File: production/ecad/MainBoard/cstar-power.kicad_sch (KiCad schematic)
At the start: 48 parts, among them IC1 LT8648SEV#PBF, J1 Conn_01x02_Pin, J2 Conn_01x02_Pin, J3 Conn_01x02_Pin, J4 XT60PW-M, U1 AZ1117IH-3.3TRG1

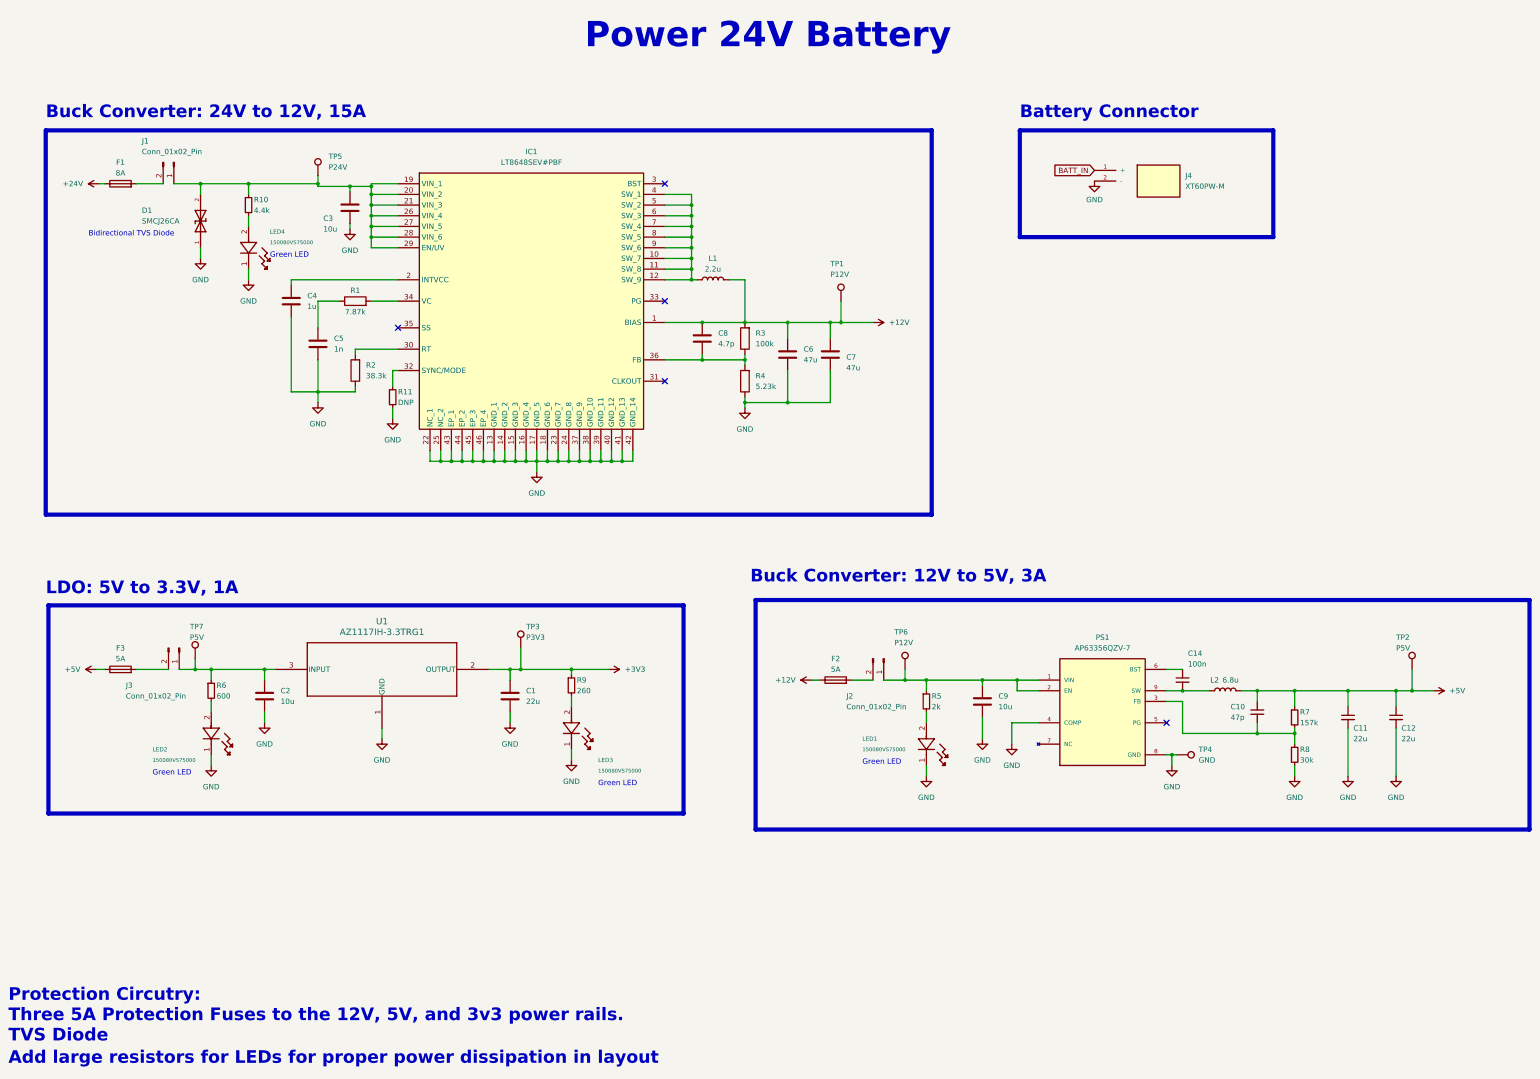
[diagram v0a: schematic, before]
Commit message: changed the path of the footprints and changed the name of the test points
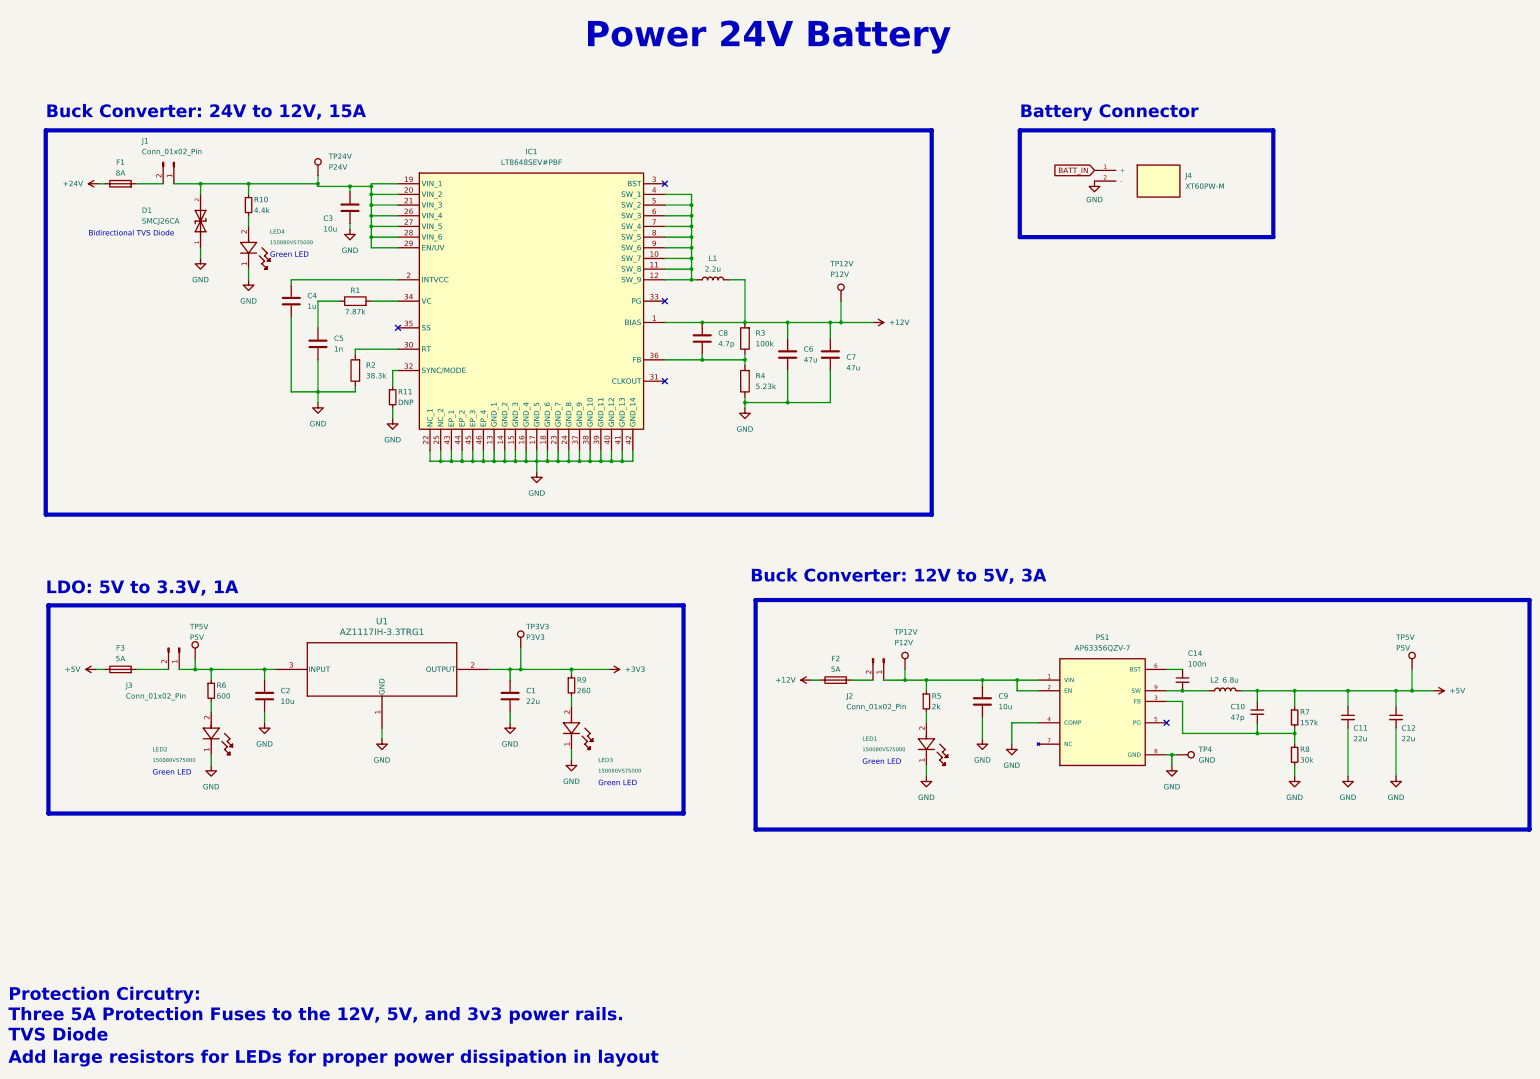
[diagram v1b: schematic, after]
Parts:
- IC1: footprint LT8648SEVPBF -> (none)
- LED1, LED2, LED3, LED4: footprint LED_0VS75000_WRE -> 150080VS75000:LED_0VS75000_WRE
- U1: footprint SOT223_AZ1117I_6P5X3P5_DIO -> AZ1117IH-3.3TRG1:SOT230P700X185-4N
- renumbered TP1 to TP12V, TP6 to TP12V, TP5 to TP24V, TP3 to TP3V3, TP2 to TP5V, TP7 to TP5V
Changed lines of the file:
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@@
       (effects (font (size 0.9 0.9)) (justify left))
     )
-    (property "Footprint" "LED_0VS75000_WRE" (at 242.57 187.96 0)
+    (property "Footprint" "150080VS75000:LED_0VS75000_WRE" (at 242.57 187.96 0)
       (effects (font (size 1.27 1.27) italic) hide)
     )
@@
   (symbol (lib_id "Connector:TestPoint") (at 97.79 57.785 0) (unit 1)
     (in_bom yes) (on_board yes) (dnp no) (fields_autoplaced)
-    (property "Reference" "TP5" (at 100.33 53.213 0)
+    (property "Reference" "TP24V" (at 100.33 53.213 0)
       (effects (font (size 1.27 1.27)) (justify left))
     )
@@
       (project "cstar-power"
         (path "/7edd775e-47a6-46f9-8e16-808bdf3a0e15"
-          (reference "TP5") (unit 1)
+          (reference "TP24V") (unit 1)
         )
       )
@@
   (symbol (lib_id "Connector:TestPoint") (at 222.25 87.63 0) (unit 1)
     (in_bom yes) (on_board yes) (dnp no)
-    (property "Reference" "TP1" (at 219.71 78.74 0)
+    (property "Reference" "TP12V" (at 219.71 78.74 0)
       (effects (font (size 1.27 1.27)) (justify left))
     )
@@
       (project "cstar-power"
         (path "/7edd775e-47a6-46f9-8e16-808bdf3a0e15"
-          (reference "TP1") (unit 1)
+          (reference "TP12V") (unit 1)
         )
       )
@@
       (effects (font (size 1.524 1.524)))
     )
-    (property "Footprint" "SOT223_AZ1117I_6P5X3P5_DIO" (at 83.82 154.94 0)
+    (property "Footprint" "AZ1117IH-3.3TRG1:SOT230P700X185-4N" (at 83.82 154.94 0)
       (effects (font (size 1.27 1.27) italic) hide)
     )
@@
       (effects (font (size 1.27 1.27)))
     )
-    (property "Footprint" "LT8648SEVPBF" (at 176.53 154.61 0)
+    (property "Footprint" "" (at 176.53 154.61 0)
       (effects (font (size 1.27 1.27)) (justify left top) hide)
     )
@@
   (symbol (lib_id "Connector:TestPoint") (at 146.05 170.18 0) (unit 1)
     (in_bom yes) (on_board yes) (dnp no)
-    (property "Reference" "TP3" (at 147.32 165.1 0)
+    (property "Reference" "TP3V3" (at 147.32 165.1 0)
       (effects (font (size 1.27 1.27)) (justify left))
     )
@@
       (project "cstar-power"
         (path "/7edd775e-47a6-46f9-8e16-808bdf3a0e15"
-          (reference "TP3") (unit 1)
+          (reference "TP3V3") (unit 1)
         )
       )
@@
       (effects (font (size 0.9 0.9)) (justify left))
     )
-    (property "Footprint" "LED_0VS75000_WRE" (at 158.115 184.15 0)
+    (property "Footprint" "150080VS75000:LED_0VS75000_WRE" (at 158.115 184.15 0)
       (effects (font (size 1.27 1.27) italic) hide)
     )
@@
   (symbol (lib_id "Connector:TestPoint") (at 358.14 175.26 0) (unit 1)
     (in_bom yes) (on_board yes) (dnp no)
-    (property "Reference" "TP2" (at 354.33 167.64 0)
+    (property "Reference" "TP5V" (at 354.33 167.64 0)
       (effects (font (size 1.27 1.27)) (justify left))
     )
@@
       (project "cstar-power"
         (path "/7edd775e-47a6-46f9-8e16-808bdf3a0e15"
-          (reference "TP2") (unit 1)
+          (reference "TP5V") (unit 1)
         )
       )
@@
       (effects (font (size 0.9 0.9)) (justify left))
     )
-    (property "Footprint" "LED_0VS75000_WRE" (at 72.39 185.42 0)
+    (property "Footprint" "150080VS75000:LED_0VS75000_WRE" (at 72.39 185.42 0)
       (effects (font (size 1.27 1.27) italic) hide)
     )
@@
       (effects (font (size 0.9 0.9)) (justify left))
     )
-    (property "Footprint" "LED_0VS75000_WRE" (at 81.28 69.85 0)
+    (property "Footprint" "150080VS75000:LED_0VS75000_WRE" (at 81.28 69.85 0)
       (effects (font (size 1.27 1.27) italic) hide)
     )
@@
   (symbol (lib_id "Connector:TestPoint") (at 68.58 172.72 0) (unit 1)
     (in_bom yes) (on_board yes) (dnp no)
-    (property "Reference" "TP7" (at 67.31 165.1 0)
+    (property "Reference" "TP5V" (at 67.31 165.1 0)
       (effects (font (size 1.27 1.27)) (justify left))
     )
@@
       (project "cstar-power"
         (path "/7edd775e-47a6-46f9-8e16-808bdf3a0e15"
-          (reference "TP7") (unit 1)
+          (reference "TP5V") (unit 1)
         )
       )
@@
   (symbol (lib_id "Connector:TestPoint") (at 237.49 175.26 0) (unit 1)
     (in_bom yes) (on_board yes) (dnp no)
-    (property "Reference" "TP6" (at 234.95 166.37 0)
+    (property "Reference" "TP12V" (at 234.95 166.37 0)
       (effects (font (size 1.27 1.27)) (justify left))
     )
@@
       (project "cstar-power"
         (path "/7edd775e-47a6-46f9-8e16-808bdf3a0e15"
-          (reference "TP6") (unit 1)
-        )
-      )
+          (reference "TP12V") (unit 1)
+        )
+      )

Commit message: footprint assignments
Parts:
- IC1: footprint (none) -> CSTAR-MainBoard-Footprints:MODULE_ESP32-WROOM-32UE_M113EH6400UH3Q0_
- LED1, LED2, LED3, LED4: footprint 150080VS75000:LED_0VS75000_WRE -> (none)
- PS1: footprint AP63356QZV-7:CONV_AP63356QZV-7 -> CSTAR-MainBoard-Footprints:USBCONN-GCT_USB4105GFA
- U1: footprint AZ1117IH-3.3TRG1:SOT230P700X185-4N -> (none)
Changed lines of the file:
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@@
       (effects (font (size 0.9 0.9)) (justify left))
     )
-    (property "Footprint" "150080VS75000:LED_0VS75000_WRE" (at 242.57 187.96 0)
+    (property "Footprint" "" (at 242.57 187.96 0)
       (effects (font (size 1.27 1.27) italic) hide)
     )
@@
       (effects (font (size 1.524 1.524)))
     )
-    (property "Footprint" "AZ1117IH-3.3TRG1:SOT230P700X185-4N" (at 83.82 154.94 0)
+    (property "Footprint" "" (at 83.82 154.94 0)
       (effects (font (size 1.27 1.27) italic) hide)
     )
@@
       (effects (font (size 1.27 1.27)))
     )
-    (property "Footprint" "" (at 176.53 154.61 0)
+    (property "Footprint" "CSTAR-MainBoard-Footprints:MODULE_ESP32-WROOM-32UE_M113EH6400UH3Q0_" (at 176.53 154.61 0)
       (effects (font (size 1.27 1.27)) (justify left top) hide)
     )
@@
       (effects (font (size 1.27 1.27)))
     )
-    (property "Footprint" "AP63356QZV-7:CONV_AP63356QZV-7" (at 284.48 185.42 0)
+    (property "Footprint" "CSTAR-MainBoard-Footprints:USBCONN-GCT_USB4105GFA" (at 284.48 185.42 0)
       (effects (font (size 1.27 1.27)) (justify bottom) hide)
     )
@@
       (effects (font (size 0.9 0.9)) (justify left))
     )
-    (property "Footprint" "150080VS75000:LED_0VS75000_WRE" (at 158.115 184.15 0)
+    (property "Footprint" "" (at 158.115 184.15 0)
       (effects (font (size 1.27 1.27) italic) hide)
     )
@@
       (effects (font (size 0.9 0.9)) (justify left))
     )
-    (property "Footprint" "150080VS75000:LED_0VS75000_WRE" (at 72.39 185.42 0)
+    (property "Footprint" "" (at 72.39 185.42 0)
       (effects (font (size 1.27 1.27) italic) hide)
     )
@@
       (effects (font (size 0.9 0.9)) (justify left))
     )
-    (property "Footprint" "150080VS75000:LED_0VS75000_WRE" (at 81.28 69.85 0)
+    (property "Footprint" "" (at 81.28 69.85 0)
       (effects (font (size 1.27 1.27) italic) hide)
     )

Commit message: footprint assign more
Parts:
- D1: footprint SMCJ26CA:DIOM7959X262N -> CSTAR-MainBoard-Footprints:SMCJSeries_LTF
- IC1: footprint CSTAR-MainBoard-Footprints:MODULE_ESP32-WROOM-32UE_M113EH6400UH3Q0_ -> CSTAR-MainBoard-Footprints:Buck-05-08-1604_ADI
- J1, J2, J3: footprint Connector_Phoenix_SPT:PhoenixContact_SPT_1.5_9-H-3.5_1x09_P3.5mm_Horizontal -> Connector_PinHeader_2.54mm:PinHeader_1x02_P2.54mm_Vertical
- J4: footprint XT60PW-M:AMASS_XT60PW-M -> CSTAR-MainBoard-Footprints:AMASS_XT60PW-M
- LED1, LED2, LED3, LED4: footprint (none) -> CSTAR-MainBoard-Footprints:LED_0VS75000_WRE
- PS1: footprint CSTAR-MainBoard-Footprints:USBCONN-GCT_USB4105GFA -> CSTAR-MainBoard-Footprints:IC9_AP63356QZV-7_DIO
- U1: footprint (none) -> CSTAR-MainBoard-Footprints:TO252-2_AZ1117ID-3.3TRG1_DIO
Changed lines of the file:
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@@
       (effects (font (size 0.9 0.9)) (justify left))
     )
-    (property "Footprint" "" (at 242.57 187.96 0)
+    (property "Footprint" "CSTAR-MainBoard-Footprints:LED_0VS75000_WRE" (at 242.57 187.96 0)
       (effects (font (size 1.27 1.27) italic) hide)
     )
@@
       (effects (font (size 1.27 1.27)) (justify left))
     )
-    (property "Footprint" "XT60PW-M:AMASS_XT60PW-M" (at 292.735 70.485 0)
+    (property "Footprint" "CSTAR-MainBoard-Footprints:AMASS_XT60PW-M" (at 292.735 70.485 0)
       (effects (font (size 1.27 1.27)) (justify bottom) hide)
     )
@@
       (effects (font (size 1.27 1.27)) (justify left))
     )
-    (property "Footprint" "Connector_Phoenix_SPT:PhoenixContact_SPT_1.5_9-H-3.5_1x09_P3.5mm_Horizontal" (at 64.77 170.18 0)
+    (property "Footprint" "Connector_PinHeader_2.54mm:PinHeader_1x02_P2.54mm_Vertical" (at 64.77 170.18 0)
       (effects (font (size 1.27 1.27)) hide)
     )
@@
       (effects (font (size 1.27 1.27)) (justify left))
     )
-    (property "Footprint" "Connector_Phoenix_SPT:PhoenixContact_SPT_1.5_9-H-3.5_1x09_P3.5mm_Horizontal" (at 63.5 54.61 0)
+    (property "Footprint" "Connector_PinHeader_2.54mm:PinHeader_1x02_P2.54mm_Vertical" (at 63.5 54.61 0)
       (effects (font (size 1.27 1.27)) hide)
     )
@@
       (effects (font (size 1.524 1.524)))
     )
-    (property "Footprint" "" (at 83.82 154.94 0)
+    (property "Footprint" "CSTAR-MainBoard-Footprints:TO252-2_AZ1117ID-3.3TRG1_DIO" (at 83.82 154.94 0)
       (effects (font (size 1.27 1.27) italic) hide)
     )
@@
       (effects (font (size 1.27 1.27)))
     )
-    (property "Footprint" "CSTAR-MainBoard-Footprints:MODULE_ESP32-WROOM-32UE_M113EH6400UH3Q0_" (at 176.53 154.61 0)
+    (property "Footprint" "CSTAR-MainBoard-Footprints:Buck-05-08-1604_ADI" (at 176.53 154.61 0)
       (effects (font (size 1.27 1.27)) (justify left top) hide)
     )
@@
       (effects (font (size 1.27 1.27)))
     )
-    (property "Footprint" "CSTAR-MainBoard-Footprints:USBCONN-GCT_USB4105GFA" (at 284.48 185.42 0)
+    (property "Footprint" "CSTAR-MainBoard-Footprints:IC9_AP63356QZV-7_DIO" (at 284.48 185.42 0)
       (effects (font (size 1.27 1.27)) (justify bottom) hide)
     )
@@
       (effects (font (size 0.9 0.9)) (justify left))
     )
-    (property "Footprint" "" (at 158.115 184.15 0)
+    (property "Footprint" "CSTAR-MainBoard-Footprints:LED_0VS75000_WRE" (at 158.115 184.15 0)
       (effects (font (size 1.27 1.27) italic) hide)
     )
@@
       (effects (font (size 0.9 0.9)) (justify left))
     )
-    (property "Footprint" "" (at 72.39 185.42 0)
+    (property "Footprint" "CSTAR-MainBoard-Footprints:LED_0VS75000_WRE" (at 72.39 185.42 0)
       (effects (font (size 1.27 1.27) italic) hide)
     )
@@
       (effects (font (size 0.9 0.9)) (justify left))
     )
-    (property "Footprint" "" (at 81.28 69.85 0)
+    (property "Footprint" "CSTAR-MainBoard-Footprints:LED_0VS75000_WRE" (at 81.28 69.85 0)
       (effects (font (size 1.27 1.27) italic) hide)
     )
@@
       (effects (font (size 1.27 1.27)) (justify left))
     )
-    (property "Footprint" "Connector_Phoenix_SPT:PhoenixContact_SPT_1.5_9-H-3.5_1x09_P3.5mm_Horizontal" (at 232.41 172.72 0)
+    (property "Footprint" "Connector_PinHeader_2.54mm:PinHeader_1x02_P2.54mm_Vertical" (at 232.41 172.72 0)
       (effects (font (size 1.27 1.27)) hide)
     )
@@
       (effects (font (size 1.27 1.27)) (justify right))
     )
-    (property "Footprint" "SMCJ26CA:DIOM7959X262N" (at 69.85 67.31 0)
-      (effects (font (size 1.27 1.27)) (justify bottom) hide)
-    )
+    (property "Footprint" "CSTAR-MainBoard-Footprints:SMCJSeries_LTF" (at 69.85 67.31 0)
+      (effects (font (size 1.27 1.27)) (justify bottom) hide)
+    )

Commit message: Inductor footprints (L1 & L2) were updated
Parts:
- L1: footprint Inductor_SMD:L_0805_2012Metric -> CSTAR-MainBoard-Footprints:L1_2.2uH
- L2: footprint Inductor_SMD:L_0805_2012Metric -> CSTAR-MainBoard-Footprints:L2_6.8uH
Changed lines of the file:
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@@
       (effects (font (size 1.27 1.27)))
     )
-    (property "Footprint" "Inductor_SMD:L_0805_2012Metric" (at 191.77 82.55 0)
+    (property "Footprint" "CSTAR-MainBoard-Footprints:L1_2.2uH" (at 191.77 82.55 0)
       (effects (font (size 1.27 1.27)) hide)
     )
@@
       (effects (font (size 1.27 1.27)))
     )
-    (property "Footprint" "Inductor_SMD:L_0805_2012Metric" (at 313.69 180.34 0)
-      (effects (font (size 1.27 1.27)) hide)
-    )
+    (property "Footprint" "CSTAR-MainBoard-Footprints:L2_6.8uH" (at 313.69 180.34 0)
+      (effects (font (size 1.27 1.27)) hide)
+    )

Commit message: fixing issue
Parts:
- C6, C7: footprint Capacitor_SMD:C_0805_2012Metric -> Capacitor_SMD:C_1206_3216Metric
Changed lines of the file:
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@@
       (effects (font (size 1.27 1.27)) (justify left))
     )
-    (property "Footprint" "Capacitor_SMD:C_0805_2012Metric" (at 220.6752 104.14 0)
+    (property "Footprint" "Capacitor_SMD:C_1206_3216Metric" (at 220.6752 104.14 0)
       (effects (font (size 1.27 1.27)) hide)
     )
@@
       (effects (font (size 1.27 1.27)) (justify left))
     )
-    (property "Footprint" "Capacitor_SMD:C_0805_2012Metric" (at 210.5152 104.14 0)
-      (effects (font (size 1.27 1.27)) hide)
-    )
+    (property "Footprint" "Capacitor_SMD:C_1206_3216Metric" (at 210.5152 104.14 0)
+      (effects (font (size 1.27 1.27)) hide)
+    )
